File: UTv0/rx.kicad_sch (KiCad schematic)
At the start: 34 parts

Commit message: Receive Circuit annotations
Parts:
- gave numbers to parts that had none: 34
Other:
- note added: "3 op-amp stages"
- note added: "peak detection (+ rectifier)"

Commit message: Transmit Circuit
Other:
- note added: "?"
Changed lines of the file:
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@@
+		)
+	)
+	(text "?"
+		(exclude_from_sim no)
+		(at 177.8 101.854 0)
+		(effects
+			(font
+				(size 1.27 1.27)
+			)
 		)
 	)
 	(global_label "-9V"
-		(shape output)
+		(shape passive)
 		(at 273.05 127 0)
 		(fields_autoplaced yes)
@@
 		)
 		(property "Intersheetrefs" "${INTERSHEET_REFS}"
-			(at 279.9057 127 0)
+			(at 278.7944 127 0)
 			(effects
 				(font
@@
 	)
 	(global_label "+9V"
-		(shape output)
+		(shape passive)
 		(at 274.32 50.8 0)
 		(fields_autoplaced yes)
@@
 		)
 		(property "Intersheetrefs" "${INTERSHEET_REFS}"
-			(at 281.1757 50.8 0)
+			(at 280.0644 50.8 0)
 			(effects
 				(font

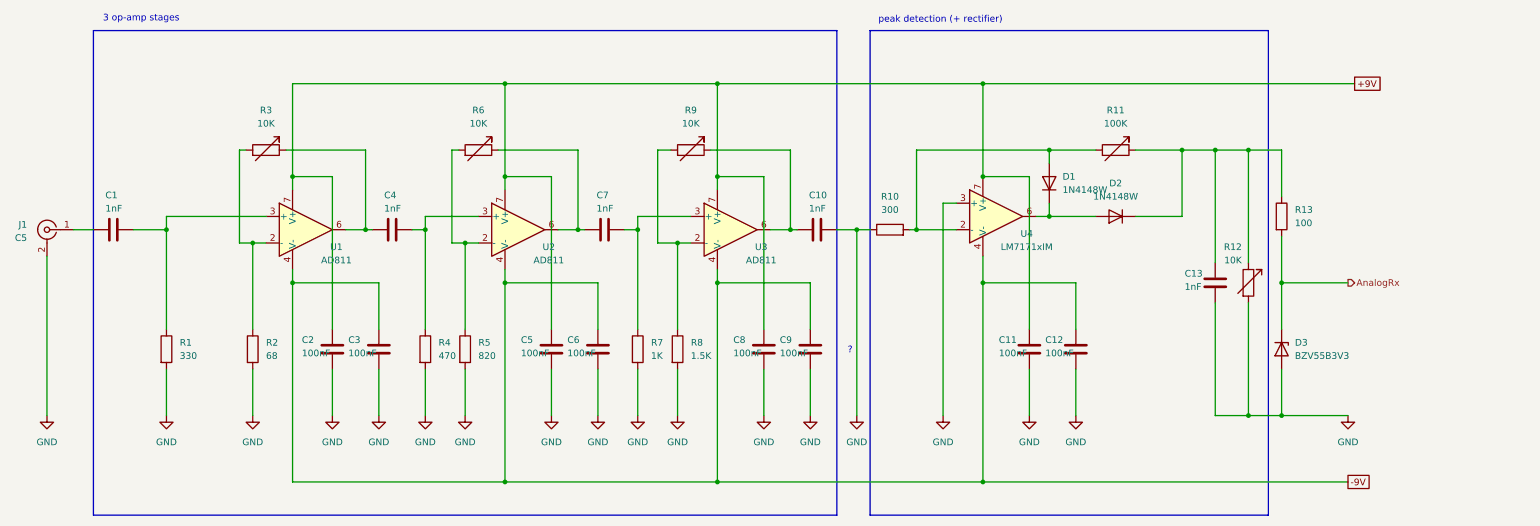
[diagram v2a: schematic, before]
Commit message: Schematic revised, initial tests started
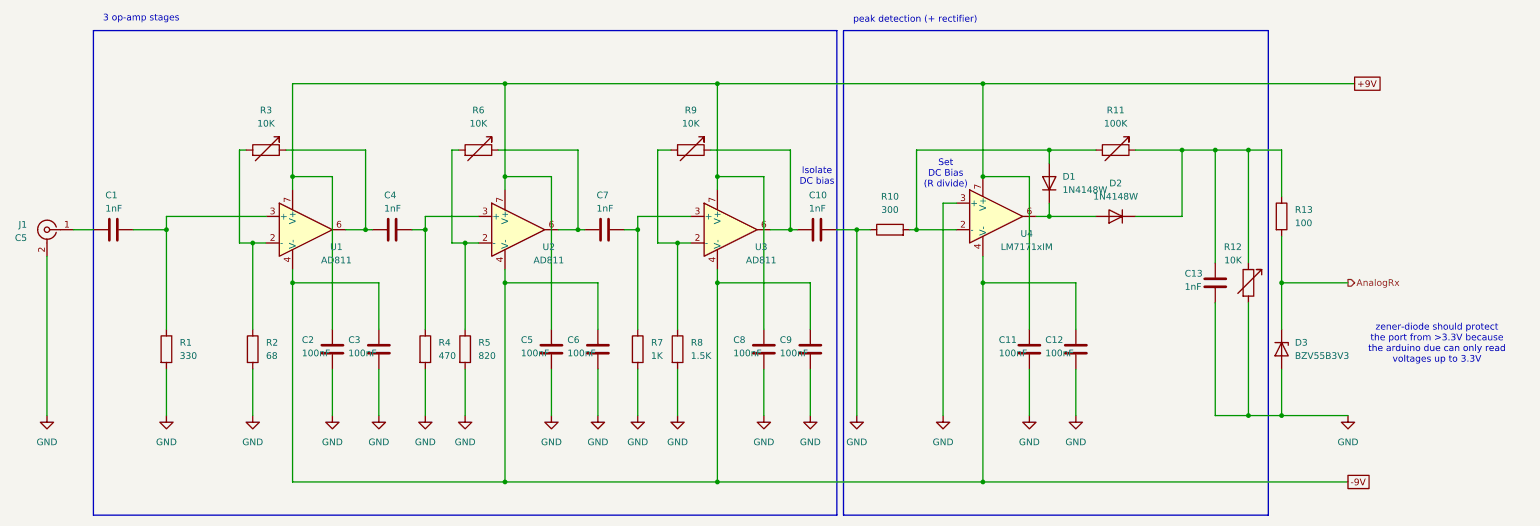
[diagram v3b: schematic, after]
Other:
- note added: "Isolate DC bias"
- note added: "Set DC Bias (R divide)"
- note added: "zener-diode should protect the port from >3.3V because the arduino due can only read voltages up to 3.3V"
- note removed: "?"
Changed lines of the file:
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@@
 	)
 	(rectangle
-		(start 181.61 40.64)
+		(start 176.53 40.64)
 		(end 257.81 133.35)
 		(stroke
@@
 		(fill
 			(type none)
+		)
+	)
+	(text "Set\nDC Bias\n(R divide)"
+		(exclude_from_sim no)
+		(at 196.088 68.072 0)
+		(effects
+			(font
+				(size 1.27 1.27)
+			)
 		)
 	)
@@
 		)
 	)
-	(text "peak detection (+ rectifier)"
+	(text "zener-diode should protect\nthe port from >3.3V because\nthe arduino due can only read\nvoltages up to 3.3V"
 		(exclude_from_sim no)
-		(at 195.072 38.608 0)
+		(at 290.068 100.584 0)
 		(effects
 			(font
@@
 		)
 	)
-	(text "?"
+	(text "peak detection (+ rectifier)"
 		(exclude_from_sim no)
-		(at 177.8 101.854 0)
+		(at 190.246 38.608 0)
 		(effects
 			(font
+				(size 1.27 1.27)
+			)
+		)
+	)
+	(text "Isolate\nDC bias"
+		(exclude_from_sim no)
+		(at 171.45 68.58 0)
+		(effects
+			(font

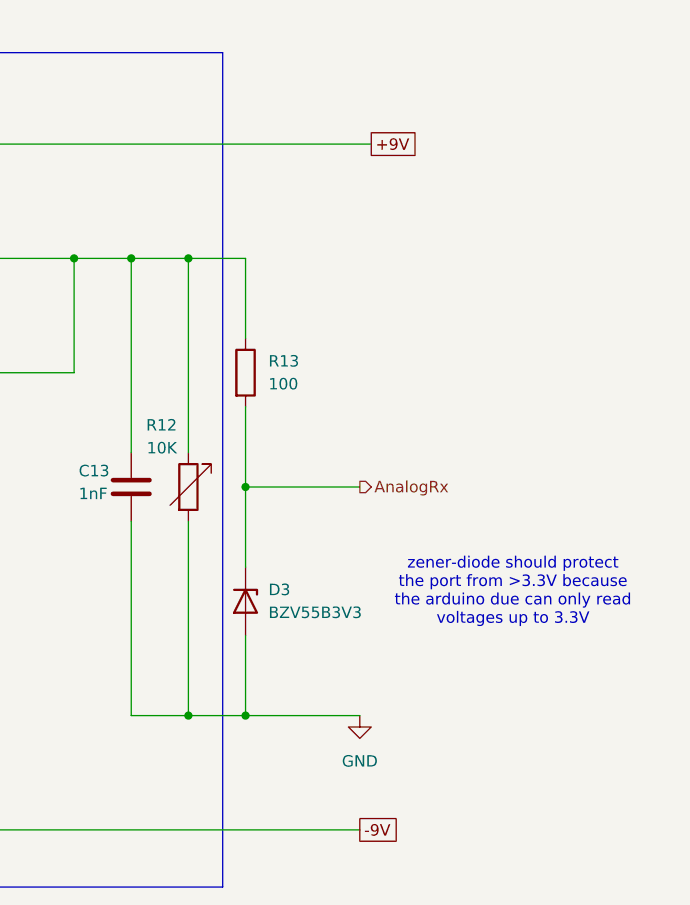
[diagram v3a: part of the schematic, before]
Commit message: v6 cleanup + back to delta (dubious), v7: new methods to detect peak + dynamic reference + thresholding (does not work), backtrack
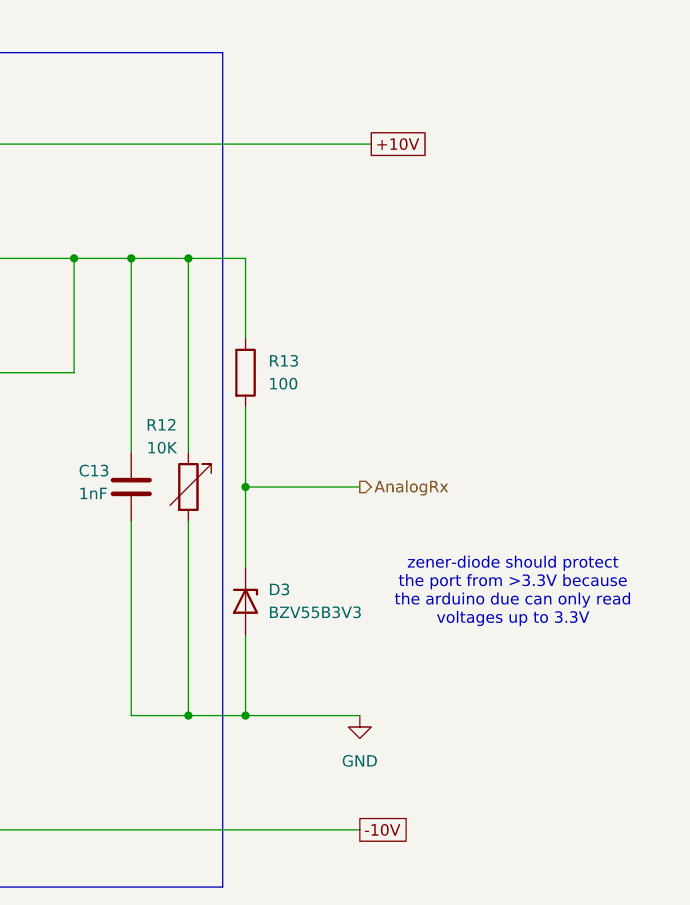
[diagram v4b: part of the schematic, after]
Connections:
- net +9V renamed +10V
- net -9V renamed -10V
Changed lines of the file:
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@@
 		)
 	)
-	(global_label "-9V"
+	(global_label "-10V"
 		(shape passive)
 		(at 273.05 127 0)
@@
 		)
 		(property "Intersheetrefs" "${INTERSHEET_REFS}"
-			(at 278.7944 127 0)
+			(at 280.0039 127 0)
 			(effects
 				(font
@@
 		)
 	)
-	(global_label "+9V"
+	(global_label "+10V"
 		(shape passive)
 		(at 274.32 50.8 0)
@@
 		)
 		(property "Intersheetrefs" "${INTERSHEET_REFS}"
-			(at 280.0644 50.8 0)
+			(at 281.2739 50.8 0)
 			(effects
 				(font
